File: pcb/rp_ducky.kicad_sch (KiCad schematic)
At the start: 34 parts, among them J1 USB_A, Q1 2N7002, SW1 R-667799, SW2 R-667799, U1 TCR2EE33, U2 W25Q32JVZP, U3 RP2040, U4 D1213A-04V, Y1 Crystal_GND24

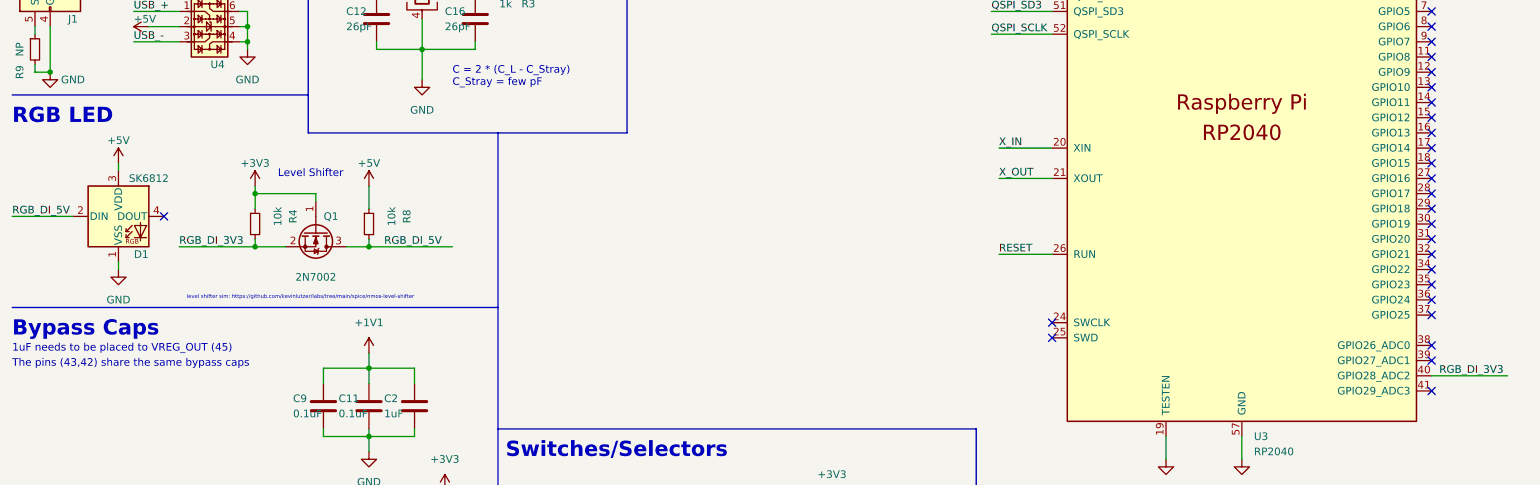
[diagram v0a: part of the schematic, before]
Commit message: remove level shifter for the SK8012 rgb led
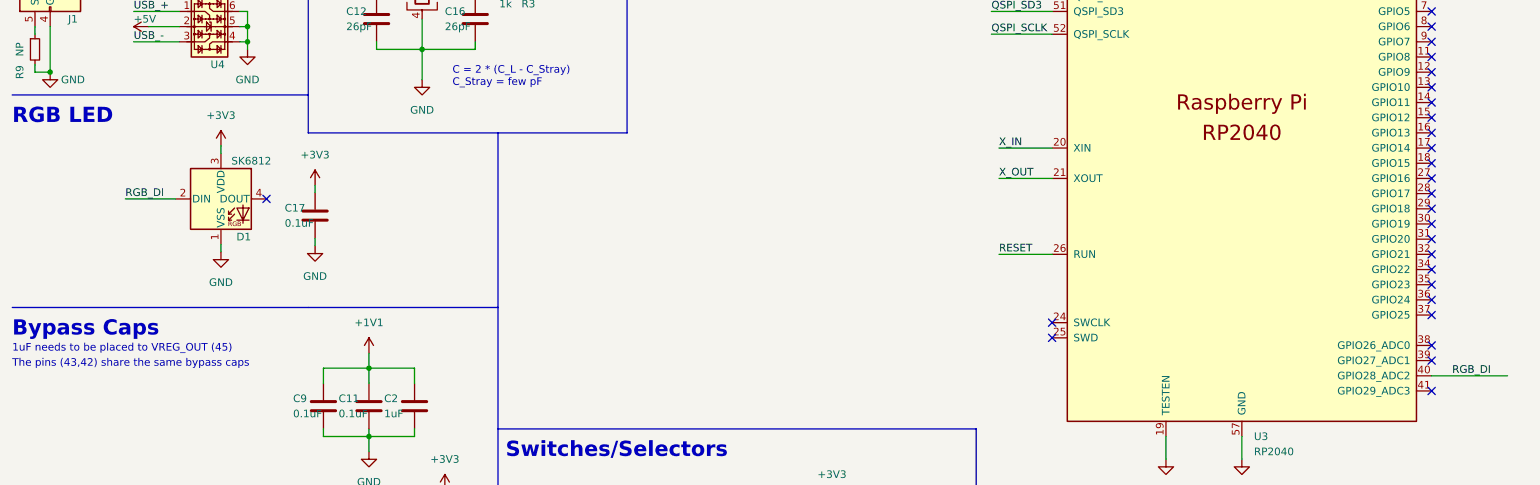
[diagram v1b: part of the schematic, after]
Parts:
- removed Q1: 2N7002, Package_TO_SOT_SMD:SOT-23, symbol Transistor_FET:2N7002
- removed R4, R8: 10k, Resistor_SMD:R_0402_1005Metric, symbol Device:R_Small
- added C17: 0.1uF, Capacitor_SMD:C_0201_0603Metric, symbol Device:C
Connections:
- net RGB_DI_5V is gone; now on net RGB_DI: D1.2 (DIN)
- net +3V3: now also D1.3 (VDD), C17.2
- net +5V: no longer D1.3 (VDD)
- net GND: now also C17.1
- net RGB_DI_3V3 renamed RGB_DI
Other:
- note removed: "Level Shifter"
- note removed: "level shifter sim: https://github.com/kevinlutzer/labs/tree/main/spice/nmos-level-shifter"
- moved on the sheet: D1

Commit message: add v4 gerbers
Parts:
- removed C17: 0.1uF, Capacitor_SMD:C_0201_0603Metric, symbol Device:C
- removed D1: SK6812, LED_SMD:LED_SK6812_EC15_1.5x1.5mm, symbol LED:SK6812
- removed R9: NP, Resistor_SMD:R_0402_1005Metric, symbol Device:R_Small
- removed U4: D1213A-04V, Package_TO_SOT_SMD:SOT-563, symbol Kevin_Lutzer_Lbr:D1213A-04V
- added D1: LED, LED_SMD:LED_0603_1608Metric, symbol Device:LED
- added JP1: SolderJumper_2_Open, Jumper:SolderJumper-2_P1.3mm_Open_TrianglePad1.0x1.5mm, symbol Jumper:SolderJumper_2_Open
- added R1: 220, Resistor_SMD:R_0402_1005Metric, symbol Device:R_Small
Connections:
- net GND: now also JP1.1 (A), R1.2
- net at J1.5 (Shield): now also JP1.2 (B)
- net RGB_DI renamed LED
- net LED: now also D1.2 (A)
- new net: D1.1 (K), R1.1
- no-connect marks 32 -> 31
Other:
- note added: "LED"
- note removed: "ESD Protection"
- note removed: "RGB LED"
- moved on the sheet: J1

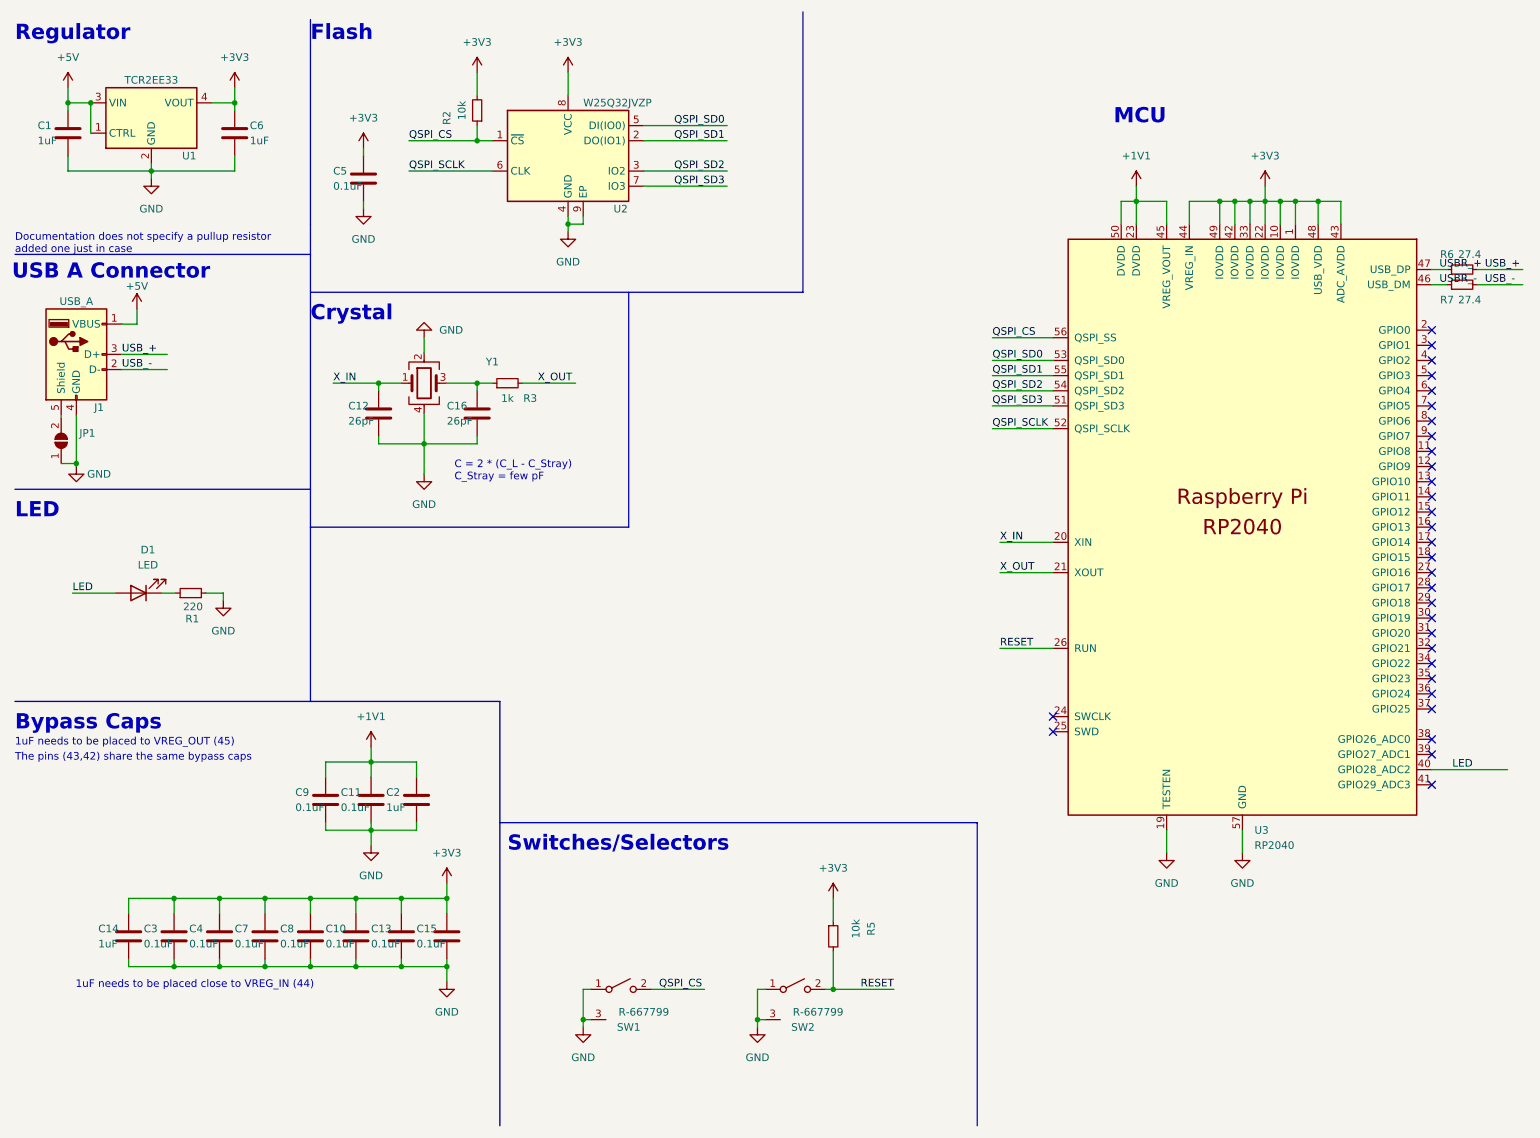
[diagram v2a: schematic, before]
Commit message: use 0402 parts only, on the bottom use larger solderable pads
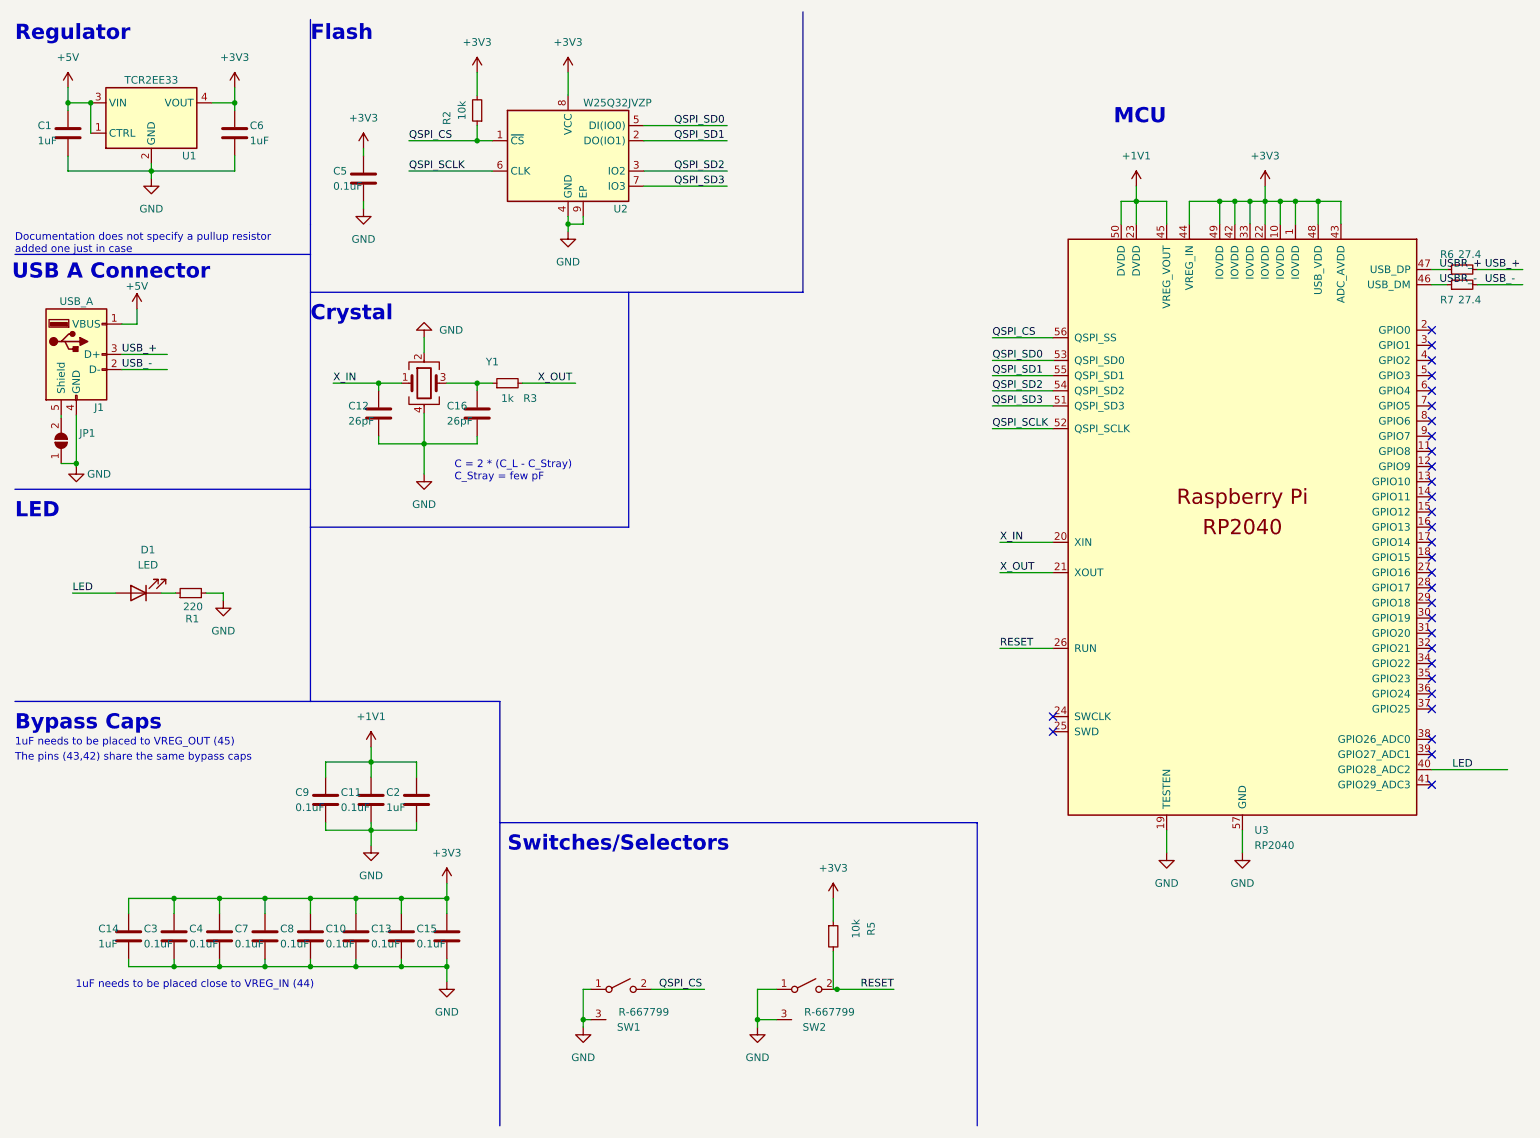
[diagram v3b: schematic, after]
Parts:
- C1, C2, C6: footprint Capacitor_SMD:C_0402_1005Metric -> Capacitor_SMD:C_0402_1005Metric_Pad0.74x0.62mm_HandSolder
- C10, C11, C15, C7, C8, C9: footprint Capacitor_SMD:C_0201_0603Metric -> Capacitor_SMD:C_0402_1005Metric_Pad0.74x0.62mm_HandSolder
- C13, C3, C4, C5: footprint Capacitor_SMD:C_0201_0603Metric -> Capacitor_SMD:C_0402_1005Metric
- R6, R7: footprint Resistor_SMD:R_0201_0603Metric -> Resistor_SMD:R_0402_1005Metric
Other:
- moved on the sheet: SW2
